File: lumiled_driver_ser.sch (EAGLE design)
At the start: 16 parts, among them X1 PWR

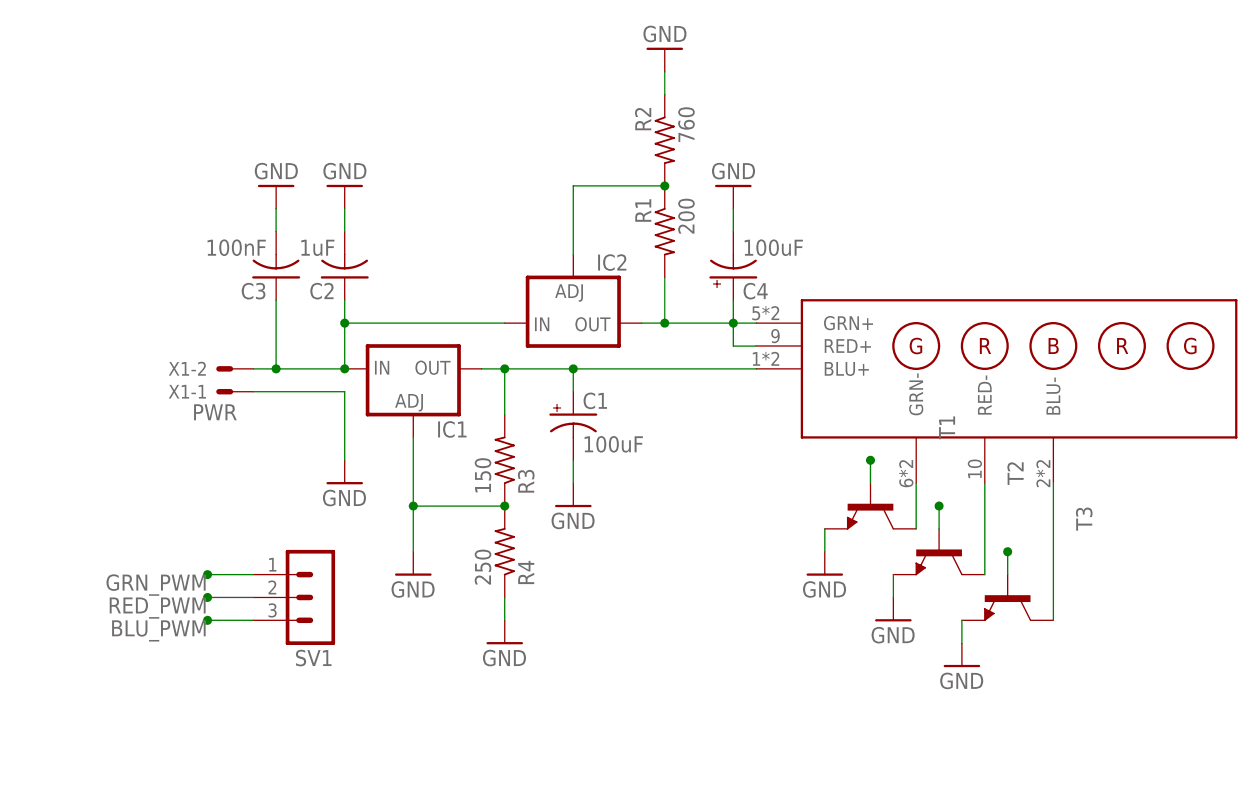
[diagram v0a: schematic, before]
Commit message: -added zener to series board -started work on board layout
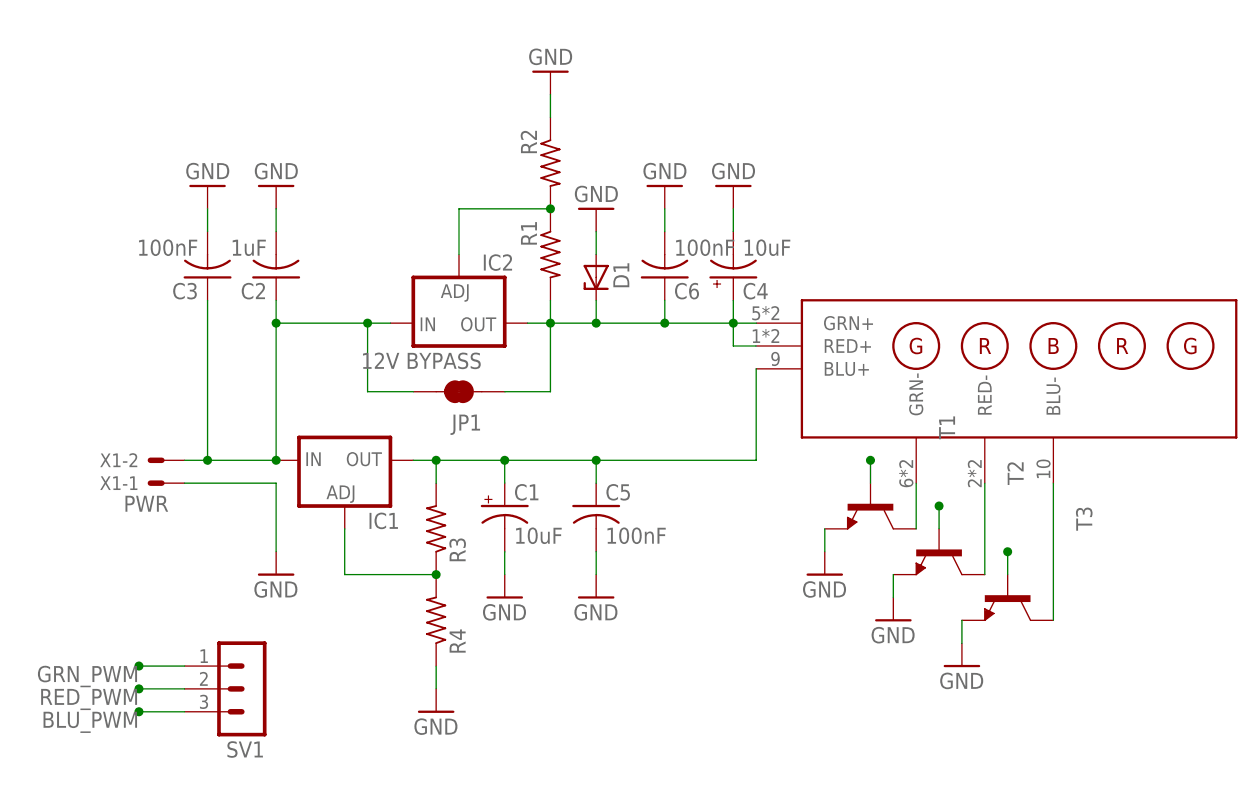
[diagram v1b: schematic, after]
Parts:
- added C5, C6: 100nF, rcl:C-US025-024X044
- added D1: (no value), diode:ZENER-DIODEC1702-15
- added JP1: 12V BYPASS, SparkFun-Jumpers:JUMPER-SMT_2_NC_TRACE_SILK
- C1, C4: value 100uF -> 10uF
- R1: value 200 -> (none)
- R2: value 760 -> (none)
- R3: value 150 -> (none)
- R4: value 250 -> (none)
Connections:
- removed net +3.3V: C1.+, IC1.OUT, R3.2, U$1.BLU+
- new net N$4: C1.+, C5.1, IC1.OUT, R3.2, U$1.BLU+
- new net N$8: IC1.ADJ, R3.1, R4.2
- net +VIN: now also JP1.2
- net GND: now also C5.2, C6.2, D1.A; no longer IC1.ADJ, R3.1, R4.2
- net N$6: now also C6.1, D1.C, JP1.1
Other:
- moved on the sheet: C1, C2, C3, IC1, IC2, R1, R2, R3, R4, SV1, X1-1, X1-2
